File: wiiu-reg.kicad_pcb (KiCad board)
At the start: 2 copper layers, 69.4 x 31.8 mm, 87 parts, among them IC1 SIC431CED-T1-GE3, IC2 SIC431CED-T1-GE3, IC3 NCP718ASNADJT1G, U1 AP62301Z6-7, U2 AP62301Z6-7, U3 AP62301Z6-7

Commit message: make thing hopefully suck less
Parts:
- added TP6: GND, TestPoint:TestPoint_Pad_2.0x2.0mm, F.Cu at (1.52, 1.52)
- moved R15 20.3 mm to (148.9, 94.5), turned to 0 degrees
- moved R16 20.3 mm to (148.9, 95.4), turned to 180 degrees
- moved C42 17.6 mm to (151.7, 96.9), turned to 0 degrees
- moved U3 16.0 mm to (151.2, 94.9), turned to 180 degrees
- moved R2 14.0 mm to (145.9, 103.4), turned to 0 degrees
- moved R5 14.0 mm to (145.9, 104.3), turned to 180 degrees
- moved GND 12.4 mm to (161.4, 97.0), turned to 90 degrees
- moved C16 11.9 mm to (148.7, 105.8), turned to 0 degrees
- moved GND 11.8 mm to (158.4, 105.9)
- moved C24 11.2 mm to (132.6, 106.5), turned to 0 degrees
- moved C41 10.6 mm to (152.9, 92.8)
- moved U1 9.79 mm to (148.2, 103.8), turned to 180 degrees
- moved C25 9.65 mm to (132.6, 105.0), turned to 0 degrees
- moved 3v3 9.62 mm to (129.5, 106.0)
- moved L5 8.36 mm to (156.5, 94.4), turned to 0 degrees
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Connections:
- C20 pad 1: +5V -> Net-(IC1-VDD)
- C21 pad 1: +5V -> Net-(IC1-VDRV)
- C39 pad 1: +5V -> Net-(IC2-VDD)
- C40 pad 1: +5V -> Net-(IC2-VDRV)
- IC1 pad 12: +5V -> Net-(IC1-VDRV)
- IC1 pad 15: +5V -> Net-(IC1-VDD)
- IC2 pad 12: +5V -> Net-(IC2-VDRV)
- IC2 pad 15: +5V -> Net-(IC2-VDD)
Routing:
- net +5V: track 105.8 -> 13.7 mm
- net VIN: track 12.6 -> 4.68 mm, vias 36 -> 30
- net +3V3: track 24.7 -> 18.4 mm, vias 3 -> 6
- net +1V5: track 6.97 -> 13.2 mm, vias 0 -> 2
- net Net-(U1-BST): track 6.69 -> 3.14 mm
- net Net-(U3-BST): track 5.46 -> 2.99 mm, vias 0 -> 2
- net Net-(U2-BST): track 5.47 -> 3.29 mm, vias 0 -> 2
- net Net-(U3-SW): track 2.07 -> 0.00 mm
- net +1V15: track 18.0 -> 16.8 mm
- net +1V25: track 4.30 -> 3.20 mm
- net Net-(IC2-VDD): track 0.00 -> 1.09 mm
- net Net-(IC1-VDD): track 0.00 -> 1.07 mm
- net Net-(IC1-VDRV): track 0.00 -> 1.04 mm
- net Net-(IC2-VDRV): track 0.00 -> 0.99 mm
- net GND: vias 151 -> 214
- added copper zone on In2.Cu, net +3V3
- added copper zone on In1.Cu, net GND
- added copper zone on In2.Cu, net VIN
- removed copper zone on B.Cu, net +3V3
- removed copper zone on B.Cu, net VIN
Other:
- board size 69.4 x 31.8 mm -> 65.9 x 31.8 mm
- copper layers 2 -> 4

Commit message: (hopefully) final layout!
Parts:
- removed TP6: GND, TestPoint:TestPoint_Pad_2.0x2.0mm
- added 3v31: 3v3, TestPoint:TestPoint_Pad_2.0x2.0mm, F.Cu at (126.5, 106.0)
- added FAN: 5v, TestPoint:TestPoint_Pad_2.0x2.0mm, F.Cu at (165.0, 99.5)
- added GND: GND, TestPoint:TestPoint_Pad_2.0x2.0mm, F.Cu at (165.0, 102.5)
- C21, C40: value 22uF -> 2.2uF
- moved C29 14.7 mm to (113.9, 90.5), turned to -90 degrees
- moved C5 14.5 mm to (145.1, 86.6), turned to -90 degrees
- moved GND 12.9 mm to (145.6, 104.6), turned to 180 degrees
- moved R5 12.3 mm to (147.1, 92.1), turned to 90 degrees
- moved R2 11.5 mm to (148.1, 92.1), turned to -90 degrees
- moved C16 11.3 mm to (145.6, 94.9), turned to -90 degrees
- moved 5v 9.98 mm to (148.6, 104.6), turned to -90 degrees
- moved U1 9.42 mm to (147.6, 94.5), turned to 90 degrees
- moved C17 8.98 mm to (151.7, 105.1), turned to 0 degrees
- moved C18 6.95 mm to (151.7, 103.7), turned to 0 degrees
- moved L2 6.43 mm to (148.2, 99.8), turned to -90 degrees
- moved C1 5.56 mm to (149.7, 96.2), turned to -90 degrees
- moved 1v5 3.73 mm to (165.0, 93.2)
- moved C41 3.73 mm to (156.6, 92.1)
- moved C42 3.73 mm to (155.3, 96.2)
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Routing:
- net +3V3: track 18.4 -> 22.0 mm
- net +1V5: track 13.2 -> 15.6 mm
- net +5V: track 13.7 -> 16.0 mm
- net +1V0: track 19.2 -> 18.0 mm
- net +1V15: track 16.8 -> 17.6 mm
- net VIN: vias 30 -> 31
- net GND: vias 214 -> 221
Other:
- outline, holes or cut-outs redrawn

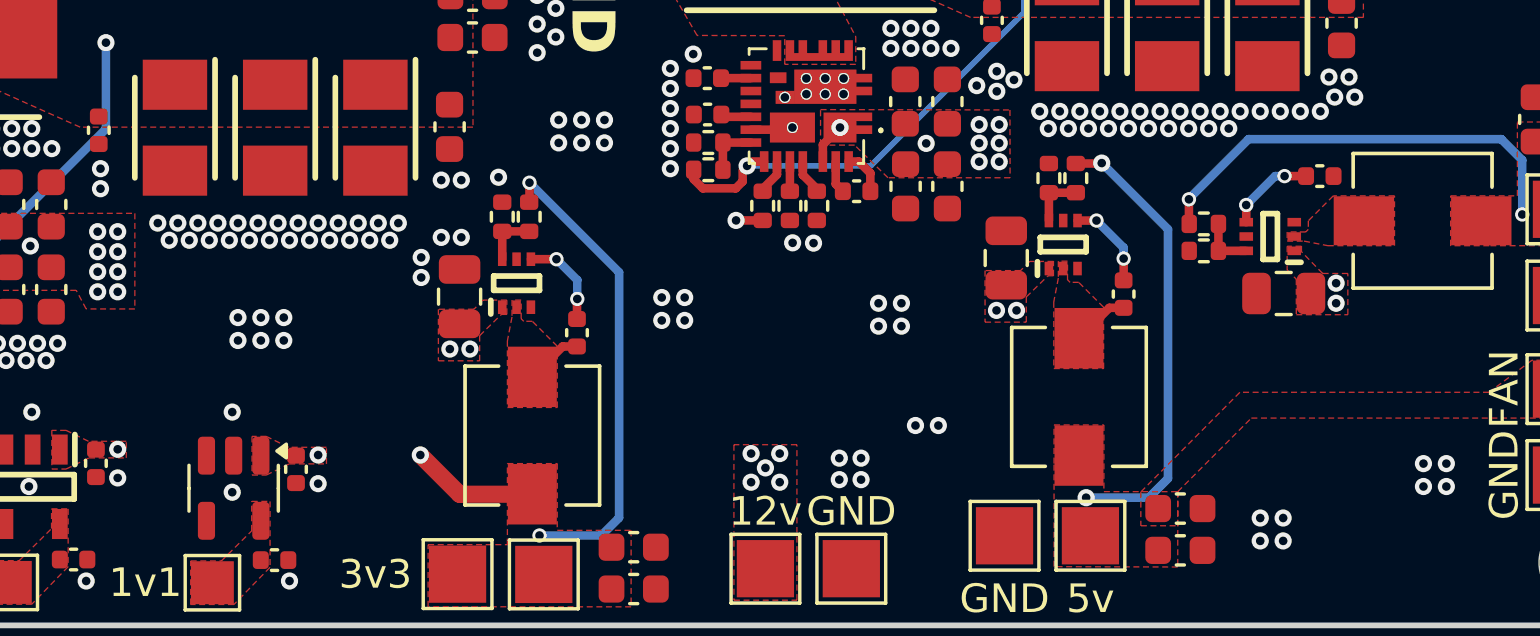
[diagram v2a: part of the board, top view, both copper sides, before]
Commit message: Fix some unrouted nets
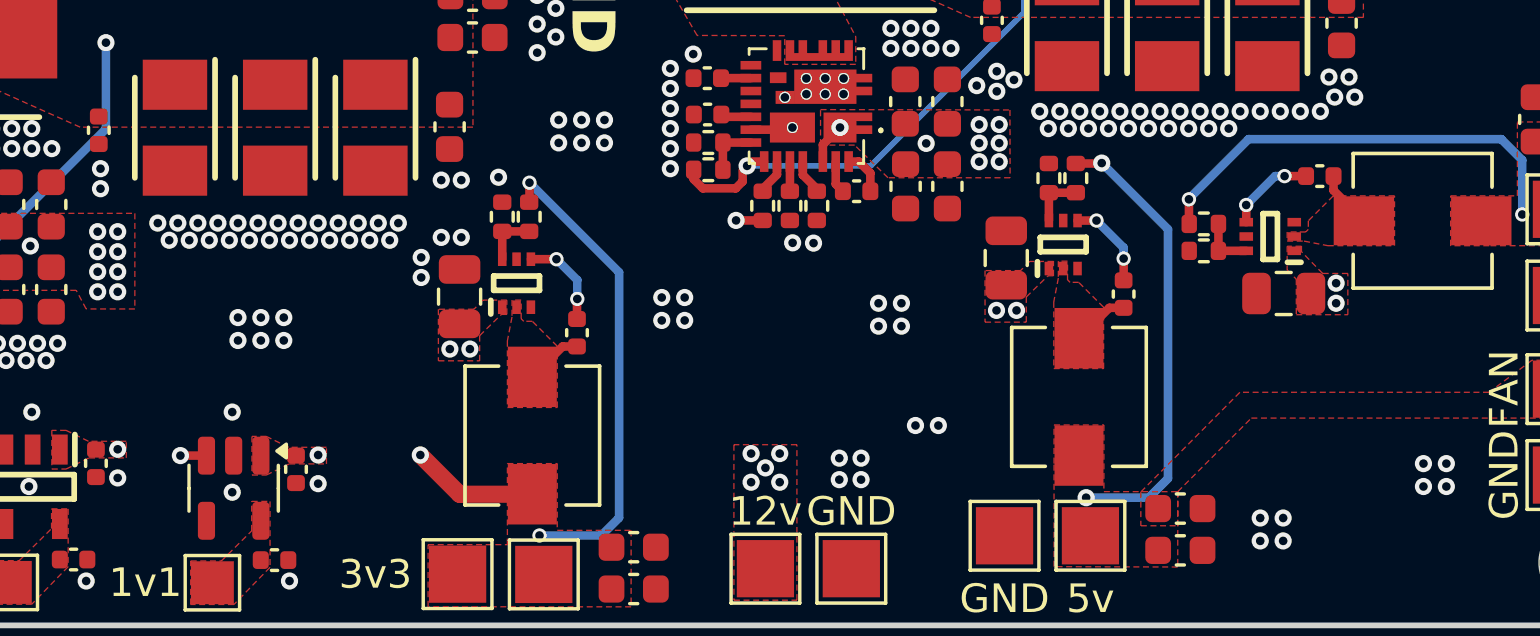
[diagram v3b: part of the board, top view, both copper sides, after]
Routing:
- net Net-(U3-SW): track 0.00 -> 2.00 mm
- net +3V3: track 22.0 -> 22.9 mm, vias 6 -> 7
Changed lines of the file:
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@@
+	)
+	(segment
+		(start 117.6975 101.82)
+		(end 117.7 101.8225)
+		(width 0.2)
+		(layer "F.Cu")
+		(net 10)
 	)
 	(segment
@@
 	)
 	(segment
+		(start 117.6875 101.81)
+		(end 117.7 101.8225)
+		(width 0.2)
+		(layer "F.Cu")
+		(net 10)
+	)
+	(segment
 		(start 128.98 92.96)
 		(end 128.97 92.97)
@@
 	)
 	(segment
+		(start 116.79 101.82)
+		(end 117.6975 101.82)
+		(width 0.3)
+		(layer "F.Cu")
+		(net 10)
+	)
+	(segment
 		(start 128.98 92.29)
 		(end 128.98 92.96)
@@
 	)
 	(via
+		(at 116.79 101.82)
+		(size 0.6)
+		(drill 0.3)
+		(layers "F.Cu" "B.Cu")
+		(free yes)
+		(net 10)
+	)
+	(via
 		(at 129.33 104.61)
 		(size 0.5)
@@
 	)
 	(segment
+		(start 157.06 92.06)
+		(end 157.06 92.56)
+		(width 0.3)
+		(layer "F.Cu")
+		(net 14)
+	)
+	(segment
+		(start 157.06 92.56)
+		(end 158.12 93.62)
+		(width 0.3)
+		(layer "F.Cu")
+		(net 14)
+	)
+	(segment

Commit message: Complete redesign
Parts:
- removed 1v5: 1v5, TestPoint:TestPoint_Pad_2.0x2.0mm
- removed 3v3, 3v31: 3v3, TestPoint:TestPoint_Pad_2.0x2.0mm
- removed 5v: 5v, TestPoint:TestPoint_Pad_2.0x2.0mm
- removed the GND at (140.2, 105.8)
- removed the GND at (165.0, 96.2)
- removed the GND at (145.6, 104.6)
- removed the GND at (165.0, 102.5)
- removed L3, L5: 3.3uH, wiiu-reg:INDM4847X300N
- removed L4: MPXV1D0840L1R0, wiiu-reg:MPXV1D0840L1R0
- removed R14: 510k, Resistor_SMD:R_0402_1005Metric
- removed R15: 8.66k, Resistor_SMD:R_0402_1005Metric
- removed R16, R17: 10k, Resistor_SMD:R_0402_1005Metric
- removed R18: 500, Resistor_SMD:R_0402_1005Metric
- added 1V5: 1v5, TestPoint:TestPoint_Pad_2.0x2.0mm, F.Cu at (161.9, 93.5)
- added 3V3: 3v3, TestPoint:TestPoint_Pad_2.0x2.0mm, F.Cu at (130.5, 108.1)
- added 5V: 5v, TestPoint:TestPoint_Pad_2.0x2.0mm, F.Cu at (145.3, 107.9)
- added C49: 1uF, Capacitor_SMD:C_0402_1005Metric, F.Cu at (112.9, 101.8)
- added C50: 1uF, Capacitor_SMD:C_0402_1005Metric, F.Cu at (112.9, 106.8)
- added GND: GND, TestPoint:TestPoint_Pad_2.0x2.0mm, F.Cu at (161.9, 101.4)
- added GND: GND, TestPoint:TestPoint_Pad_2.0x2.0mm, F.Cu at (107.0, 98.9)
- added GND: GND, TestPoint:TestPoint_Pad_2.0x2.0mm, F.Cu at (148.3, 107.9)
- added GND: GND, TestPoint:TestPoint_Pad_2.0x2.0mm, F.Cu at (161.9, 96.5)
- C1: value 100nF -> F930J107KBA; footprint Capacitor_SMD:C_0402_1005Metric -> wiiu-reg:F930J107KBA; moved to B.Cu
- C10, C11, C5: moved to B.Cu
- C16: value 10uF -> 0.1uF; footprint Capacitor_SMD:C_0805_2012Metric -> Capacitor_SMD:C_0402_1005Metric
- C17, C33: value 22uF -> 1uF; footprint Capacitor_SMD:C_0603_1608Metric -> Capacitor_SMD:C_0402_1005Metric
- C18, C34: value 22uF -> 2.2uF; footprint Capacitor_SMD:C_0603_1608Metric -> Capacitor_SMD:C_0402_1005Metric
- C19: value 0.1uF -> F930J107KBA; footprint Capacitor_SMD:C_0402_1005Metric -> wiiu-reg:F930J107KBA
- C20: value 1uF -> F930J107KBA; footprint Capacitor_SMD:C_0402_1005Metric -> wiiu-reg:F930J107KBA
- C21: value 2.2uF -> F930J107KBA; footprint Capacitor_SMD:C_0402_1005Metric -> wiiu-reg:F930J107KBA; moved to B.Cu
- C22: value 100nF -> 0.1uF
- C23: value 10uF -> 0.1uF; footprint Capacitor_SMD:C_0805_2012Metric -> Capacitor_SMD:C_0402_1005Metric; moved to B.Cu
- C26, C27, C28: value F930J107KBA -> 22uF; footprint wiiu-reg:F930J107KBA -> Capacitor_SMD:C_0603_1608Metric
- C29, C38: value 0.1uF -> 22uF; footprint Capacitor_SMD:C_0402_1005Metric -> Capacitor_SMD:C_0603_1608Metric
- C32: value 22uF -> 0.1uF; footprint Capacitor_SMD:C_0603_1608Metric -> Capacitor_SMD:C_0402_1005Metric
- C39, C45, C46: value 1uF -> 22uF; footprint Capacitor_SMD:C_0402_1005Metric -> Capacitor_SMD:C_0603_1608Metric
- C4: value F930J107KBA -> 0.1uF; footprint wiiu-reg:F930J107KBA -> Capacitor_SMD:C_0402_1005Metric
- C40: value 2.2uF -> 22uF; footprint Capacitor_SMD:C_0402_1005Metric -> Capacitor_SMD:C_0603_1608Metric
- C41: value 100nF -> 22uF; footprint Capacitor_SMD:C_0402_1005Metric -> Capacitor_SMD:C_0603_1608Metric
- C42: value 10uF -> 22uF; footprint Capacitor_SMD:C_0805_2012Metric -> Capacitor_SMD:C_0603_1608Metric
- IC3: value NCP718ASNADJT1G -> TPS7A26125DRVR; footprint wiiu-reg:NCP718ASNADJT1G -> wiiu-reg:TPS7A26125DRVR
- L2: value 3.3uH -> MPXV1D0840L1R0; footprint wiiu-reg:INDM4847X300N -> wiiu-reg:MPXV1D0840L1R0
- R10, R4, R5: value 10k -> 510k
- R11: value 100k -> 7.5k; footprint Resistor_SMD:R_0402_1005Metric -> Resistor_SMD:R_1206_3216Metric
- R12: value 12k -> 2.61k; footprint Resistor_SMD:R_0402_1005Metric -> Resistor_SMD:R_1206_3216Metric
- R13: value 510k -> 1.58k; footprint Resistor_SMD:R_0402_1005Metric -> Resistor_SMD:R_1206_3216Metric
- R2: value 52.3k -> 100k
- R3: value 100k -> 10k
- R6: value 510k -> 11k
- R7: value 510k -> 100k
- R8: value 31.6k -> 12k
- R9: value 11k -> 510k
- U1, U2, U3: value AP62301Z6-7 -> ~; footprint wiiu-reg:AP62301Z6-7 -> wiiu-reg:Reggie
- moved C38 50.6 mm to (159.7, 94.3), turned to -90 degrees
- moved C36 49.1 mm to (159.7, 97.3)
- moved C35 47.4 mm to (158.2, 97.3), turned to 90 degrees
- moved R11 46.0 mm to (151.6, 101.4), turned to 0 degrees
- moved C37 46.0 mm to (158.2, 94.3), turned to -90 degrees
- moved L2 35.7 mm to (116.6, 83.1), turned to 0 degrees
- moved C41 32.9 mm to (127.5, 107.3), turned to 180 degrees
- moved 12v 31.8 mm to (107.0, 95.9), turned to 180 degrees
- moved C43 31.3 mm to (139.3, 107.2), turned to 0 degrees
- moved C44 30.9 mm to (139.3, 108.6), turned to 0 degrees
- moved C42 30.6 mm to (127.5, 108.8), turned to 180 degrees
- moved C46 29.4 mm to (142.3, 108.6), turned to 180 degrees
- moved R6 29.1 mm to (109.9, 92.2), turned to 0 degrees
- moved C45 28.9 mm to (142.3, 107.2), turned to 180 degrees
- moved R13 27.7 mm to (135.2, 100.5)
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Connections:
- net 1v SW renamed Net-(IC1-SW_1)
- C1 pad 1: Net-(U1-BST) -> +1V0
- C1 pad 2: Net-(U1-SW) -> GND
- C16 pad 1: GND -> Net-(IC1-BOOT)
- C16 pad 2: VIN -> Net-(IC1-PHASE)
- C17 pad 1: +5V -> Net-(IC1-VDD)
- C18 pad 1: +5V -> Net-(IC1-VDRV)
- C19 pad 1: Net-(IC1-BOOT) -> +1V15
- C19 pad 2: Net-(IC1-PHASE) -> GND
- C20 pad 1: Net-(IC1-VDD) -> +1V15
- C21 pad 1: Net-(IC1-VDRV) -> +1V15
- C22 pad 1: Net-(U2-BST) -> +1V15
- C22 pad 2: Net-(U2-SW) -> GND
- C23 pad 1: GND -> +1V15
- C23 pad 2: VIN -> GND
- C24 pad 1: +3V3 -> +1V15
- C25 pad 1: +3V3 -> +1V15
- C28 pad 1: +1V15 -> VIN
- C29 pad 1: +1V15 -> VIN
- C30 pad 1: +1V15 -> VIN
- C31 pad 1: +1V15 -> VIN
- C32 pad 1: +1V15 -> Net-(IC2-BOOT)
- C32 pad 2: GND -> Net-(IC2-PHASE)
- C33 pad 1: +1V15 -> Net-(IC2-VDD)
- C34 pad 1: VIN -> Net-(IC2-VDRV)
- C37 pad 1: VIN -> +1V5
- C38 pad 1: Net-(IC2-BOOT) -> +1V5
- C38 pad 2: Net-(IC2-PHASE) -> GND
- C39 pad 1: Net-(IC2-VDD) -> VIN
- C40 pad 1: Net-(IC2-VDRV) -> VIN
- C41 pad 1: Net-(U3-BST) -> +3V3
- C41 pad 2: Net-(U3-SW) -> GND
- C42 pad 1: GND -> +3V3
- C42 pad 2: VIN -> GND
- C43 pad 1: +1V5 -> VIN
- C44 pad 1: +1V5 -> VIN
- C45 pad 1: +3V3 -> +5V
- C46 pad 1: +1V25 -> +5V
- C47 pad 1: +3V3 -> +1V25
- C48 pad 1: +1V1 -> +3V3
- IC2 pad 30: 1v15 SW -> Net-(IC2-SW_1)
- IC2 pad 31: 1v15 SW -> Net-(IC2-SW_1)
- IC2 pad 32: 1v15 SW -> Net-(IC2-SW_1)
- IC2 pad 33: 1v15 SW -> Net-(IC2-SW_1)
- IC2 pad 5: 1v15 SW -> Net-(IC2-SW_1)
- IC2 pad 6: 1v15 SW -> Net-(IC2-SW_1)
- IC2 pad 7: 1v15 SW -> Net-(IC2-SW_1)
- IC2 pad 8: 1v15 SW -> Net-(IC2-SW_1)
- IC2 pad 9: 1v15 SW -> Net-(IC2-SW_1)
- IC3 pad 1: +3V3 -> +1V25
- IC3 pad 3: +3V3 -> GND
- IC3 pad 4: Net-(IC3-NC/ADJ) -> +3V3
- IC3 pad 5: +1V25 -> GND
- L2 pad 1: Net-(U1-SW) -> Net-(IC2-SW_1)
- L2 pad 2: +5V -> +1V15
- R10 pad 1: Net-(U2-FB) -> Net-(IC2-MODE2)
- R11 pad 1: VIN -> Net-(U1-FB)
- R11 pad 2: Net-(IC2-EN) -> GND
- R12 pad 1: Net-(IC2-FB) -> Net-(U2-FB)
- R13 pad 1: Net-(IC2-MODE1) -> Net-(U3-FB)
- R2 pad 1: +5V -> VIN
- R2 pad 2: Net-(U1-FB) -> Net-(IC1-EN)
- R3 pad 1: VIN -> Net-(IC1-FB)
- R3 pad 2: Net-(IC1-EN) -> GND
- R4 pad 1: Net-(IC1-FB) -> Net-(IC1-MODE1)
- R5 pad 1: Net-(U1-FB) -> Net-(IC1-MODE2)
- R6 pad 1: Net-(IC1-MODE1) -> +1V15
- R6 pad 2: GND -> Net-(IC2-FB)
- R7 pad 1: Net-(IC1-MODE2) -> VIN
- R7 pad 2: GND -> Net-(IC2-EN)
- R8 pad 1: +3V3 -> Net-(IC2-FB)
- R8 pad 2: Net-(U2-FB) -> GND
- R9 pad 1: +1V15 -> Net-(IC2-MODE1)
- R9 pad 2: Net-(IC2-FB) -> GND
- U1 pad 2: Net-(U1-SW) -> +1V5
- U1 pad 4: Net-(U1-BST) -> Net-(U1-FB)
- U2 pad 2: Net-(U2-SW) -> +3V3
- U2 pad 4: Net-(U2-BST) -> Net-(U2-FB)
- U3 pad 2: Net-(U3-SW) -> +5V
- U3 pad 4: Net-(U3-BST) -> Net-(U3-FB)
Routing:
- net +3V3: track 22.9 -> 0.65 mm, vias 7 -> 8
- net +5V: track 16.0 -> 0.00 mm, vias 2 -> 0
- net +1V5: track 15.6 -> 0.00 mm, vias 2 -> 0
- net Net-(U2-BST): track 3.29 -> 0.00 mm, vias 2 -> 0
- net +1V25: track 3.20 -> 0.00 mm
- net Net-(U1-BST): track 3.14 -> 0.00 mm, vias 2 -> 0
- net Net-(U3-BST): track 2.99 -> 0.00 mm, vias 2 -> 0
- net Net-(IC3-NC/ADJ): track 2.11 -> 0.00 mm
- net Net-(U2-SW): track 2.03 -> 0.00 mm
- net Net-(U3-SW): track 2.00 -> 0.00 mm
- net Net-(U1-SW): track 2.00 -> 0.00 mm
- net GND: track 1.59 -> 0.00 mm, vias 221 -> 434
- net +1V15: track 17.6 -> 18.7 mm, vias 2 -> 9
- net +1V0: track 18.0 -> 19.0 mm, vias 2 -> 22
- net Net-(U1-FB): track 1.91 -> 2.84 mm
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- added copper zone on B.Cu, net +1V0
- added copper zone on B.Cu, net +1V15
- added copper zone on In1.Cu, net +3V3
- added copper zone on In2.Cu, net GND
- added copper zone on F.Cu, net Net-(IC2-SW_1)
- added copper zone on In1.Cu, net VIN
- removed copper zone on In2.Cu, net +3V3
- removed copper zone on F.Cu, net 1v15 SW
- removed copper zone on In1.Cu, net GND
- removed copper zone on F.Cu, net Net-(U1-SW)
- removed copper zone on F.Cu, net Net-(U2-SW)
- removed copper zone on F.Cu, net Net-(U3-SW)
- removed copper zone on In2.Cu, net VIN
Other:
- board size 65.9 x 31.8 mm -> 60 x 32 mm
- board text removed: "PiiSU Lazr 2025 Name by pbanj"

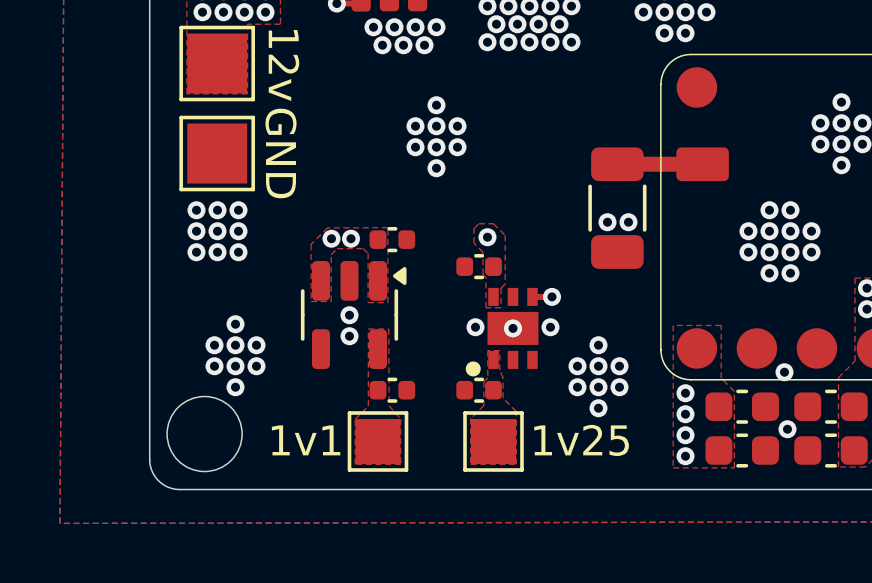
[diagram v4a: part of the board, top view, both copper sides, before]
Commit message: Forgot to add label silkscreen on the bottom
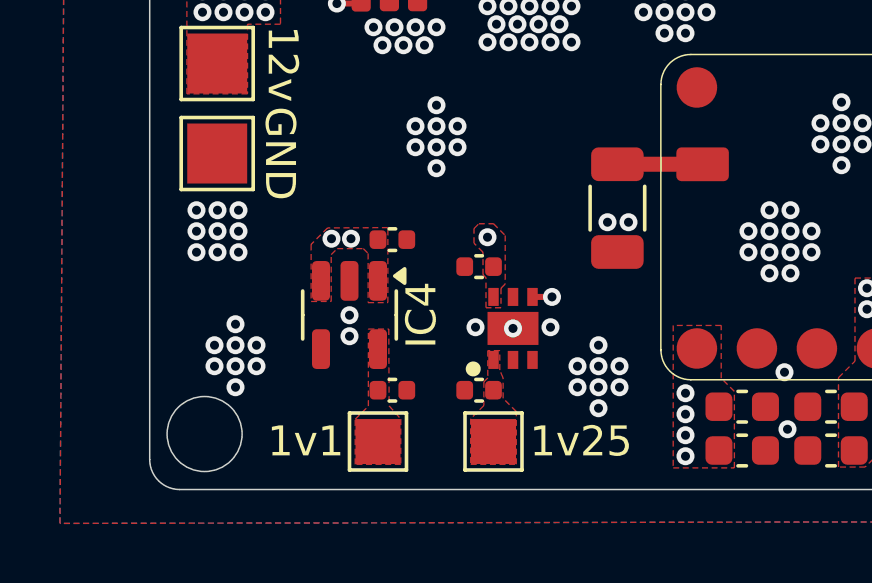
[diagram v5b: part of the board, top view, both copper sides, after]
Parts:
- IC1, IC2: value SIC431CED-T1-GE3 -> SIC431AED-T1-GE3; footprint wiiu-reg:SIC431CEDT1GE3 -> wiiu-reg:SIC431AEDT1GE3
- IC4: value ~ -> TCR2EF11,LM(CT
- U1, U2, U3: value ~ -> Reggie
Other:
- board text added: "PiiSU Lazr 2025 Name by pbanj"
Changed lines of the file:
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@@
 		(sheetname "/Low Power/")
 		(sheetfile "Low Power.kicad_sch")
-		(attr exclude_from_pos_files)
+		(attr exclude_from_pos_files exclude_from_bom)
 		(fp_line
 			(start 1.2 -1.2)
@@
 		(sheetfile "wiiu-reg.kicad_sch")
 		(clearance 0.05)
-		(attr exclude_from_pos_files)
+		(attr exclude_from_pos_files exclude_from_bom)
 		(fp_line
 			(start 1.2 1.2)
@@
 		(sheetname "/")
 		(sheetfile "wiiu-reg.kicad_sch")
-		(attr exclude_from_pos_files)
+		(attr exclude_from_pos_files exclude_from_bom)
 		(fp_line
 			(start 1.2 1.2)
@@
 		(sheetname "/Low Power/")
 		(sheetfile "Low Power.kicad_sch")
-		(attr exclude_from_pos_files)
+		(attr exclude_from_pos_files exclude_from_bom)
 		(fp_line
 			(start -1.2 1.2)
@@
 		(sheetname "/Low Power/")
 		(sheetfile "Low Power.kicad_sch")
-		(attr exclude_from_pos_files)
+		(attr exclude_from_pos_files exclude_from_bom)
 		(fp_line
 			(start -1.2 -1.2)
@@
 		(sheetname "/Low Power/")
 		(sheetfile "Low Power.kicad_sch")
-		(attr exclude_from_pos_files)
+		(attr exclude_from_pos_files exclude_from_bom)
 		(fp_line
 			(start -1.2 1.2)
@@
 			)
 		)
-		(property "Value" "~"
+		(property "Value" "Reggie"
 			(at 0 1 90)
 			(unlocked yes)
@@
 			)
 		)
-		(property "Value" "~"
+		(property "Value" "Reggie"
 			(at 0 1 0)
 			(unlocked yes)
@@
 			(at 0 -2.4 90)
 			(layer "F.SilkS")
-			(hide yes)
 			(effects
 				(font
@@
 			)
 		)
-		(property "Value" "~"
+		(property "Value" "TCR2EF11,LM(CT"
 			(at 0 2.4 90)
 			(layer "F.Fab")
@@
 		(sheetname "/Low Power/")
 		(sheetfile "Low Power.kicad_sch")
-		(attr exclude_from_pos_files)
+		(attr exclude_from_pos_files exclude_from_bom)
 		(fp_line
 			(start 1.2 -1.2)
@@
 			)
 		)
-		(property "Value" "~"
+		(property "Value" "Reggie"
 			(at 0 1 0)
 			(unlocked yes)
@@
 		(sheetname "/Low Power/")
 		(sheetfile "Low Power.kicad_sch")
-		(attr exclude_from_pos_files)
+		(attr exclude_from_pos_files exclude_from_bom)
 		(fp_line
 			(start -1.2 -1.2)
@@
 		(sheetfile "DRH.kicad_sch")
 		(clearance 0.05)
-		(attr exclude_from_pos_files)
+		(attr exclude_from_pos_files exclude_from_bom)
 		(fp_line
 			(start -0.95 -0.95)
@@
 		(sheetname "/DRH/")
 		(sheetfile "DRH.kicad_sch")
-		(attr exclude_from_pos_files)
+		(attr exclude_from_pos_files exclude_from_bom)
 		(fp_line
 			(start -0.95 -0.95)
@@
 		(embedded_fonts no)
 	)
-	(footprint "wiiu-reg:SIC431CEDT1GE3"
+	(footprint "wiiu-reg:SIC431AEDT1GE3"
 		(layer "F.Cu")
 		(at 113.342 89.94 180)
-		(descr "SIC431CED-T1-GE3-2")
+		(descr "SIC431AED-T1-GE3-2")
 		(tags "Integrated Circuit")
 		(property "Reference" "IC2"
@@
 			)
 		)
-		(property "Value" "SIC431CED-T1-GE3"
+		(property "Value" "SIC431AED-T1-GE3"
 			(at 0 0 180)
 			(layer "F.SilkS")
@@
 			)
 		)
-		(property "Mouser Part Number" "78-SIC431CED-T1-GE3"
+		(property "Mouser Part Number" "78-SIC431AED-T1-GE3"
 			(at 0 0 180)
 			(unlocked yes)
@@
 			)
 		)
-		(property "Mouser Price/Stock" "https://www.mouser.co.uk/ProductDetail/Vishay-Siliconix/SIC431CED-T1-GE3?qs=w%2Fv1CP2dgqqOLTwelPFnAg%3D%3D"
+		(property "Mouser Price/Stock" ""
 			(at 0 0 180)
 			(unlocked yes)
@@
 			)
 		)
-		(property "Manufacturer_Part_Number" "SIC431CED-T1-GE3"
+		(property "Manufacturer_Part_Number" "SIC431AED-T1-GE3"
 			(at 0 0 180)
 			(unlocked yes)
@@
 		(sheetname "/SiC431 1v15/")
 		(sheetfile "SiC431 1v15.kicad_sch")
+		(clearance 0.01)
 		(attr smd)
 		(fp_line
@@
 		(sheetname "/Low Power/")
 		(sheetfile "Low Power.kicad_sch")
-		(attr exclude_from_pos_files)
+		(attr exclude_from_pos_files exclude_from_bom)
 		(fp_line
 			(start -1.2 -1.2)
@@
 		(embedded_fonts no)
 	)
-	(footprint "wiiu-reg:SIC431CEDT1GE3"
+	(footprint "wiiu-reg:SIC431AEDT1GE3"
 		(layer "F.Cu")
 		(at 137.262 89.51 180)
-		(descr "SIC431CED-T1-GE3-2")
+		(descr "SIC431AED-T1-GE3-2")
 		(tags "Integrated Circuit")
 		(property "Reference" "IC1"
@@
 			)
 		)
-		(property "Value" "SIC431CED-T1-GE3"
+		(property "Value" "SIC431AED-T1-GE3"
 			(at 0 0 180)
 			(layer "F.SilkS")
@@
 			)
 		)
-		(property "Datasheet" "https://www.vishay.com/docs/74589/sic431.pdf"
+		(property "Datasheet" ""
 			(at 0 0 180)
 			(layer "F.Fab")
@@
 			)
 		)
-		(property "Description" "Switching Voltage Regulators microBUCK 4.5-55V; 20A"
+		(property "Description" ""
 			(at 0 0 180)
 			(layer "F.Fab")
@@
 			)
 		)
-		(property "Mouser Part Number" "78-SIC431CED-T1-GE3"
+		(property "Mouser Part Number" "78-SIC431AED-T1-GE3"
 			(at 0 0 180)
 			(unlocked yes)
@@
 			)
 		)
-		(property "Mouser Price/Stock" "https://www.mouser.co.uk/ProductDetail/Vishay-Siliconix/SIC431CED-T1-GE3?qs=w%2Fv1CP2dgqqOLTwelPFnAg%3D%3D"
+		(property "Mouser Price/Stock" ""
 			(at 0 0 180)
 			(unlocked yes)
@@
 			)
 		)
-		(property "Manufacturer_Part_Number" "SIC431CED-T1-GE3"
+		(property "Manufacturer_Part_Number" "SIC431AED-T1-GE3"
 			(at 0 0 180)
 			(unlocked yes)
@@
 		(sheetname "/SiC431 1v/")
 		(sheetfile "SiC431 1v.kicad_sch")
+		(clearance 0.01)
 		(attr smd)
 		(fp_line
@@
 		(layer "Edge.Cuts")
 	)
+	(gr_text "PiiSU \nLazr 2025\nName by pbanj"
+		(at 159.59 86.43 0)
+		(layer "B.SilkS")
+		(effects
+			(font
+				(size 0.5 0.5)
+				(thickness 0.1)
+			)
+			(justify left bottom mirror)
+		)
+	)
 	(gr_text "GND"
